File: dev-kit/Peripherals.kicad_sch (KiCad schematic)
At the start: 49 parts, among them IC201 APDS-9306-065, IC202 RV-8263-C8, IC203 BMI270, IC204 LIS2MDLTR, IC205 BMP581, IC206 DRV2603RUNT, J201 Jumper, J202 Jumper, J203 Jumper, J204 Jumper, J205 Jumper, J206 Jumper, M201 Vibrator DC Motor, Q201 DMG1013UW-7, Q202 PMZ550UNEYL, Q203 PMZ550UNEYL, X201 Power, X202 I2S, X203 Power, X204 I2C, X205 Power, X206 Power, X207 Power, X208 Power, X209 Power, X210 Motor

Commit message: Issue #117
Signed-off-by: Daniel Kampert <DanielKampert@kampis-elektroecke.de>
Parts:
- X201, X203, X205, X206, X207, X208, X209: footprint Connector_PinHeader_2.54mm:PinHeader_1x02_P2.54mm_Vertical_SMD_Pin1Left -> Connector_PinHeader_2.54mm:PinHeader_1x02_P2.54mm_Vertical_SMD_Pin1Right
- X202: footprint Connector_PinHeader_2.54mm:PinHeader_1x05_P2.54mm_Vertical_SMD_Pin1Left -> Connector_PinHeader_2.54mm:PinHeader_1x05_P2.54mm_Vertical_SMD_Pin1Right
- X204: footprint Connector_PinHeader_2.54mm:PinHeader_1x04_P2.54mm_Vertical_SMD_Pin1Left -> Connector_PinHeader_2.54mm:PinHeader_1x04_P2.54mm_Vertical_SMD_Pin1Right
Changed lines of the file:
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@@
 		(title "Watch-HW")
 		(date "2025-05-09")
-		(rev "0")
+		(rev "2")
 		(company "https://github.com/ZSWatch/Watch-HW")
 	)
@@
 			)
 		)
-		(property "Footprint" "Connector_PinHeader_2.54mm:PinHeader_1x02_P2.54mm_Vertical_SMD_Pin1Left"
+		(property "Footprint" "Connector_PinHeader_2.54mm:PinHeader_1x02_P2.54mm_Vertical_SMD_Pin1Right"
 			(at 280.67 143.51 0)
 			(effects
@@
 			)
 		)
-		(property "Footprint" "Connector_PinHeader_2.54mm:PinHeader_1x02_P2.54mm_Vertical_SMD_Pin1Left"
+		(property "Footprint" "Connector_PinHeader_2.54mm:PinHeader_1x02_P2.54mm_Vertical_SMD_Pin1Right"
 			(at 271.78 232.41 0)
 			(effects
@@
 			)
 		)
-		(property "Footprint" "Connector_PinHeader_2.54mm:PinHeader_1x02_P2.54mm_Vertical_SMD_Pin1Left"
+		(property "Footprint" "Connector_PinHeader_2.54mm:PinHeader_1x02_P2.54mm_Vertical_SMD_Pin1Right"
 			(at 91.44 223.52 0)
 			(effects
@@
 			)
 		)
-		(property "Footprint" "Connector_PinHeader_2.54mm:PinHeader_1x02_P2.54mm_Vertical_SMD_Pin1Left"
+		(property "Footprint" "Connector_PinHeader_2.54mm:PinHeader_1x02_P2.54mm_Vertical_SMD_Pin1Right"
 			(at 344.17 193.04 0)
 			(effects
@@
 			)
 		)
-		(property "Footprint" "Connector_PinHeader_2.54mm:PinHeader_1x05_P2.54mm_Vertical_SMD_Pin1Left"
+		(property "Footprint" "Connector_PinHeader_2.54mm:PinHeader_1x05_P2.54mm_Vertical_SMD_Pin1Right"
 			(at 83.82 189.23 0)
 			(effects
@@
 			)
 		)
-		(property "Footprint" "Connector_PinHeader_2.54mm:PinHeader_1x02_P2.54mm_Vertical_SMD_Pin1Left"
+		(property "Footprint" "Connector_PinHeader_2.54mm:PinHeader_1x02_P2.54mm_Vertical_SMD_Pin1Right"
 			(at 195.58 223.52 0)
 			(effects
@@
 			)
 		)
-		(property "Footprint" "Connector_PinHeader_2.54mm:PinHeader_1x02_P2.54mm_Vertical_SMD_Pin1Left"
+		(property "Footprint" "Connector_PinHeader_2.54mm:PinHeader_1x02_P2.54mm_Vertical_SMD_Pin1Right"
 			(at 205.74 146.05 0)
 			(effects
@@
 			)
 		)
-		(property "Footprint" "Connector_PinHeader_2.54mm:PinHeader_1x02_P2.54mm_Vertical_SMD_Pin1Left"
+		(property "Footprint" "Connector_PinHeader_2.54mm:PinHeader_1x02_P2.54mm_Vertical_SMD_Pin1Right"
 			(at 38.1 168.91 0)
 			(effects
@@
 			)
 		)
-		(property "Footprint" "Connector_PinHeader_2.54mm:PinHeader_1x04_P2.54mm_Vertical_SMD_Pin1Left"
+		(property "Footprint" "Connector_PinHeader_2.54mm:PinHeader_1x04_P2.54mm_Vertical_SMD_Pin1Right"
 			(at 133.35 189.23 0)
 			(effects

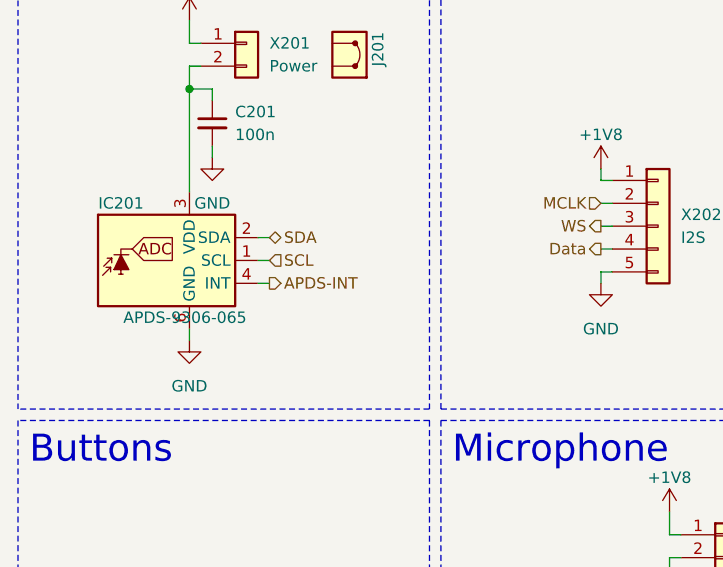
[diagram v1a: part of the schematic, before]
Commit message: Task: Issue #122
Signed-off-by: Daniel Kampert <DanielKampert@kampis-elektroecke.de>
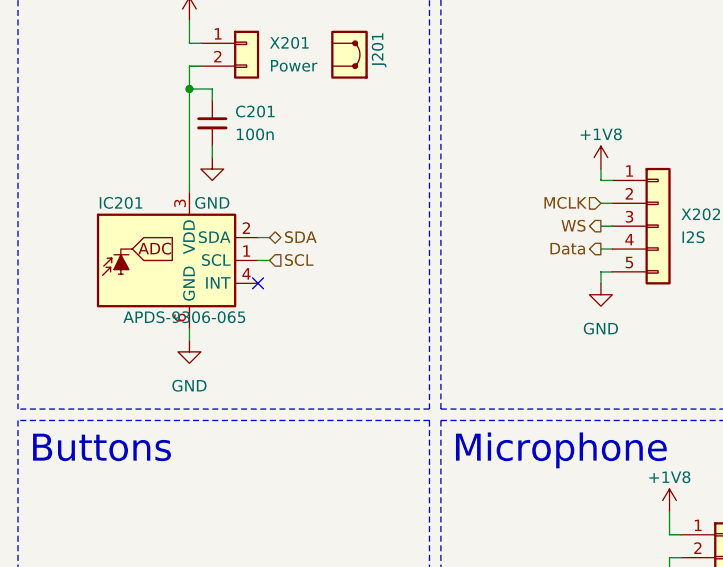
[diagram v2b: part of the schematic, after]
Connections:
- net APDS-INT: no longer names the net of IC201.4 (INT)
- no-connect marks 9 -> 10
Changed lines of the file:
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@@
+	)
+	(no_connect
+		(at 39.37 195.58)
 	)
 	(no_connect
@@
 		(pts
 			(xy 181.61 170.18) (xy 179.07 170.18)
-		)
-		(stroke
-			(width 0)
-			(type default)
-		)
-	)
-	(wire
-		(pts
-			(xy 39.37 195.58) (xy 40.64 195.58)
 		)
 		(stroke
@@
 		)
 	)
-	(hierarchical_label "APDS-INT"
-		(shape output)
-		(at 40.64 195.58 0)
-		(effects
-			(font
-				(size 1.27 1.27)
-			)
-			(justify left)
-		)
-	)

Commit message: Bug: Issue #121
Signed-off-by: Daniel Kampert <DanielKampert@kampis-elektroecke.de>
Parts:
- X201, X203, X205, X206, X207, X208, X209: footprint Connector_PinHeader_2.54mm:PinHeader_1x02_P2.54mm_Vertical_SMD_Pin1Right -> Connector_PinHeader_2.54mm:PinHeader_1x02_P2.54mm_Vertical; manf# 10129380-902001BLF -> 77311-818-02LF; mouser# 649-1012938090201BLF -> 649-77311-818-02LF
- X202: footprint Connector_PinHeader_2.54mm:PinHeader_1x05_P2.54mm_Vertical_SMD_Pin1Right -> Connector_PinHeader_2.54mm:PinHeader_1x05_P2.54mm_Vertical; manf# 10129380-905002ALF -> 77311-818-05LF; mouser# 649-10129380-905002ALF -> 649-77311-818-05LF
- X204: footprint Connector_PinHeader_2.54mm:PinHeader_1x04_P2.54mm_Vertical_SMD_Pin1Right -> Connector_PinHeader_2.54mm:PinHeader_1x04_P2.54mm_Vertical; manf# 10129380-904002ALF -> 77311-818-02LF; mouser# 649-10129380-904002ALF -> 649-77311-818-02LF
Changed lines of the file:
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@@
 			)
 		)
-		(property "Footprint" "Connector_PinHeader_2.54mm:PinHeader_1x02_P2.54mm_Vertical_SMD_Pin1Right"
+		(property "Footprint" "Connector_PinHeader_2.54mm:PinHeader_1x02_P2.54mm_Vertical"
 			(at 280.67 143.51 0)
 			(effects
@@
 			)
 		)
-		(property "manf#" "10129380-902001BLF"
+		(property "manf#" "77311-818-02LF"
 			(at 280.67 143.51 0)
 			(effects
@@
 			)
 		)
-		(property "mouser#" "649-1012938090201BLF"
+		(property "mouser#" "649-77311-818-02LF"
 			(at 280.67 143.51 0)
 			(effects
@@
 			)
 		)
-		(property "Footprint" "Connector_PinHeader_2.54mm:PinHeader_1x02_P2.54mm_Vertical_SMD_Pin1Right"
+		(property "Footprint" "Connector_PinHeader_2.54mm:PinHeader_1x02_P2.54mm_Vertical"
 			(at 271.78 232.41 0)
 			(effects
@@
 			)
 		)
-		(property "manf#" "10129380-902001BLF"
+		(property "manf#" "77311-818-02LF"
 			(at 271.78 232.41 0)
 			(effects
@@
 			)
 		)
-		(property "mouser#" "649-1012938090201BLF"
+		(property "mouser#" "649-77311-818-02LF"
 			(at 271.78 232.41 0)
 			(effects
@@
 			)
 		)
-		(property "Footprint" "Connector_PinHeader_2.54mm:PinHeader_1x02_P2.54mm_Vertical_SMD_Pin1Right"
+		(property "Footprint" "Connector_PinHeader_2.54mm:PinHeader_1x02_P2.54mm_Vertical"
 			(at 91.44 223.52 0)
 			(effects
@@
 			)
 		)
-		(property "manf#" "10129380-902001BLF"
+		(property "manf#" "77311-818-02LF"
 			(at 91.44 223.52 0)
 			(effects
@@
 			)
 		)
-		(property "mouser#" "649-1012938090201BLF"
+		(property "mouser#" "649-77311-818-02LF"
 			(at 91.44 223.52 0)
 			(effects
@@
 			)
 		)
-		(property "Footprint" "Connector_PinHeader_2.54mm:PinHeader_1x02_P2.54mm_Vertical_SMD_Pin1Right"
+		(property "Footprint" "Connector_PinHeader_2.54mm:PinHeader_1x02_P2.54mm_Vertical"
 			(at 344.17 193.04 0)
 			(effects
@@
 			)
 		)
-		(property "manf#" "10129380-902001BLF"
+		(property "manf#" "77311-818-02LF"
 			(at 344.17 193.04 0)
 			(effects
@@
 			)
 		)
-		(property "mouser#" "649-1012938090201BLF"
+		(property "mouser#" "649-77311-818-02LF"
 			(at 344.17 193.04 0)
 			(effects
@@
 			)
 		)
-		(property "Footprint" "Connector_PinHeader_2.54mm:PinHeader_1x05_P2.54mm_Vertical_SMD_Pin1Right"
+		(property "Footprint" "Connector_PinHeader_2.54mm:PinHeader_1x05_P2.54mm_Vertical"
 			(at 83.82 189.23 0)
 			(effects
@@
 			)
 		)
-		(property "Datasheet" "https://cdn.amphenol-cs.com/media/wysiwyg/files/documentation/datasheet/boardwiretoboard/bwb_econostik_254headers.pdf"
+		(property "Datasheet" "https://www.mouser.de/datasheet/2/18/2/bwb_bergstik-3370040.pdf"
 			(at 83.82 189.23 0)
 			(effects
@@
 			)
 		)
-		(property "manf#" "10129380-905002ALF"
+		(property "manf#" "77311-818-05LF"
 			(at 83.82 189.23 0)
 			(effects
@@
 			)
 		)
-		(property "mouser#" "649-10129380-905002ALF"
+		(property "mouser#" "649-77311-818-05LF"
 			(at 83.82 189.23 0)
 			(effects
@@
 			)
 		)
-		(property "Footprint" "Connector_PinHeader_2.54mm:PinHeader_1x02_P2.54mm_Vertical_SMD_Pin1Right"
+		(property "Footprint" "Connector_PinHeader_2.54mm:PinHeader_1x02_P2.54mm_Vertical"
 			(at 195.58 223.52 0)
 			(effects
@@
 			)
 		)
-		(property "manf#" "10129380-902001BLF"
+		(property "manf#" "77311-818-02LF"
 			(at 195.58 223.52 0)
 			(effects
@@
 			)
 		)
-		(property "mouser#" "649-1012938090201BLF"
+		(property "mouser#" "649-77311-818-02LF"
 			(at 195.58 223.52 0)
 			(effects
@@
 			)
 		)
-		(property "Footprint" "Connector_PinHeader_2.54mm:PinHeader_1x02_P2.54mm_Vertical_SMD_Pin1Right"
+		(property "Footprint" "Connector_PinHeader_2.54mm:PinHeader_1x02_P2.54mm_Vertical"
 			(at 205.74 146.05 0)
 			(effects
@@
 			)
 		)
-		(property "manf#" "10129380-902001BLF"
+		(property "manf#" "77311-818-02LF"
 			(at 205.74 146.05 0)
 			(effects
@@
 			)
 		)
-		(property "mouser#" "649-1012938090201BLF"
+		(property "mouser#" "649-77311-818-02LF"
 			(at 205.74 146.05 0)
 			(effects
@@
 			)
 		)
-		(property "Footprint" "Connector_PinHeader_2.54mm:PinHeader_1x02_P2.54mm_Vertical_SMD_Pin1Right"
+		(property "Footprint" "Connector_PinHeader_2.54mm:PinHeader_1x02_P2.54mm_Vertical"
 			(at 38.1 168.91 0)
 			(effects
@@
 			)
 		)
-		(property "manf#" "10129380-902001BLF"
+		(property "manf#" "77311-818-02LF"
 			(at 38.1 168.91 0)
 			(effects
@@
 			)
 		)
-		(property "mouser#" "649-1012938090201BLF"
+		(property "mouser#" "649-77311-818-02LF"
 			(at 38.1 168.91 0)
 			(effects
@@
 			)
 		)
-		(property "Footprint" "Connector_PinHeader_2.54mm:PinHeader_1x04_P2.54mm_Vertical_SMD_Pin1Right"
+		(property "Footprint" "Connector_PinHeader_2.54mm:PinHeader_1x04_P2.54mm_Vertical"
 			(at 133.35 189.23 0)
 			(effects
@@
 			)
 		)
-		(property "Datasheet" "https://cdn.amphenol-cs.com/media/wysiwyg/files/documentation/datasheet/boardwiretoboard/bwb_econostik_254headers.pdf"
+		(property "Datasheet" "https://www.mouser.de/datasheet/2/18/2/bwb_bergstik-3370040.pdf"
 			(at 133.35 189.23 0)
 			(effects
@@
 			)
 		)
-		(property "manf#" "10129380-904002ALF"
+		(property "manf#" "77311-818-02LF"
 			(at 133.35 189.23 0)
 			(effects
@@
 			)
 		)
-		(property "mouser#" "649-10129380-904002ALF"
+		(property "mouser#" "649-77311-818-02LF"
 			(at 133.35 189.23 0)
 			(effects

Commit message: Task: Issue #123
Signed-off-by: Daniel Kampert <DanielKampert@kampis-elektroecke.de>
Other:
- moved on the sheet: C201, C202, C203, C204, C205, C206, C207, C208, C209, C210, C211, IC201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
